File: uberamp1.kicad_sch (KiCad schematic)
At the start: 8 parts

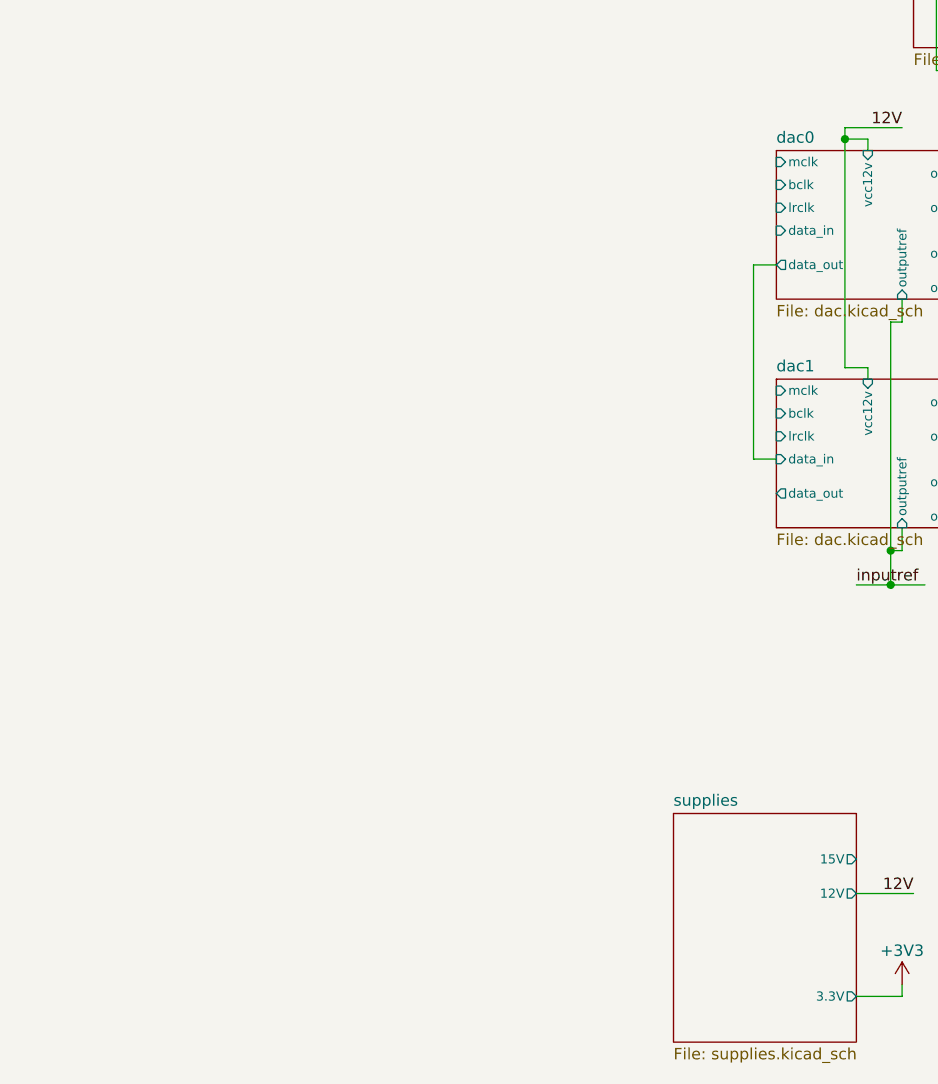
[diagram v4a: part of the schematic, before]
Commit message: add clock source to schematic
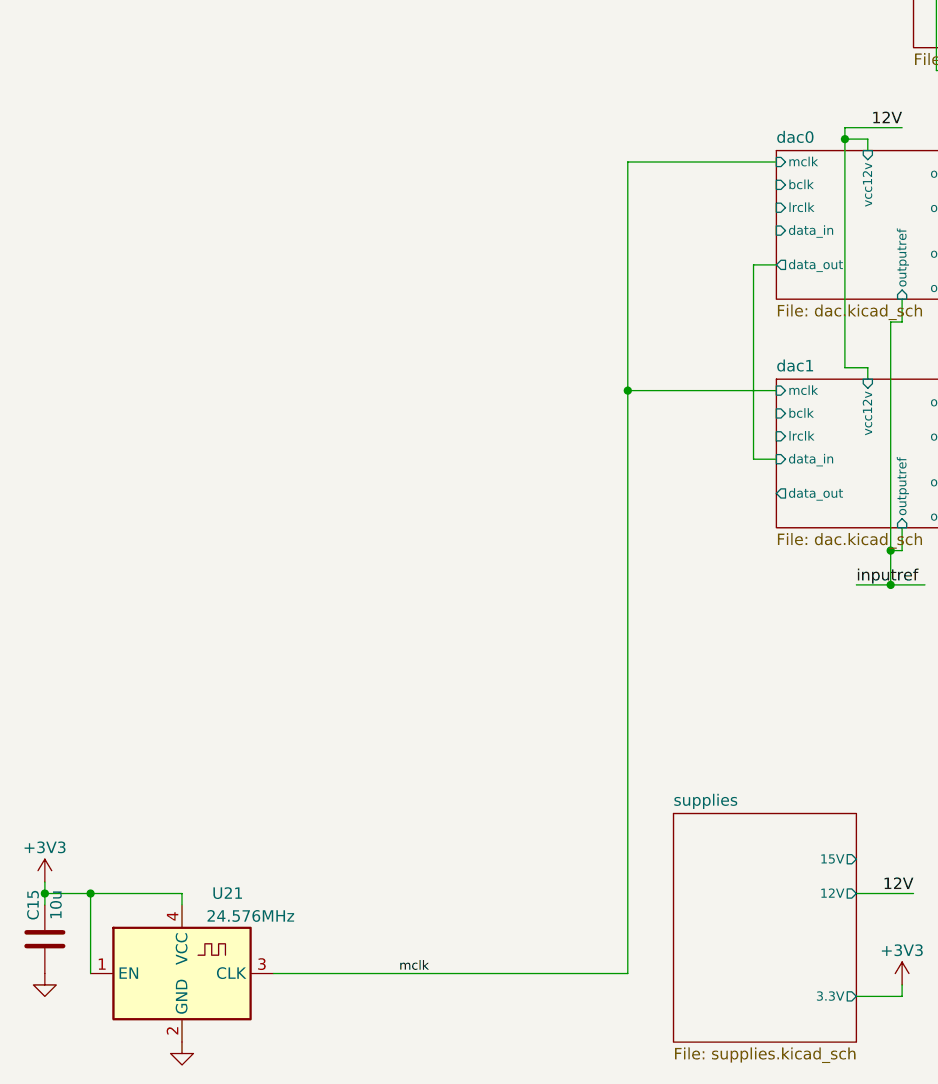
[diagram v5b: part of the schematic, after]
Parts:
- added C15: 10u, invendelirium_audio:C_0603, symbol Device:C
- added U21: 24.576MHz, symbol invendelirium_ic:kyocera_KC
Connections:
- net +3V3: now also C15.2, U21.1 (EN), U21.4 (VCC)
- net GND: now also C15.1, U21.2 (GND)
- new net mclk: U21.3 (CLK)
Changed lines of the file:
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@@
   (junction (at 186.69 113.03) (diameter 0) (color 0 0 0 0)
   )
+  (junction (at 119.38 111.76) (diameter 0) (color 0 0 0 0)
+  )
   (junction (at 209.55 92.71) (diameter 0) (color 0 0 0 0)
   )
@@
   (junction (at 210.82 21.59) (diameter 0) (color 0 0 0 0)
   )
+  (junction (at 54.61 167.64) (diameter 0) (color 0 0 0 0)
+  )
   (junction (at 189.23 76.2) (diameter 0) (color 0 0 0 0)
   )
@@
   )
   (junction (at 214.63 90.17) (diameter 0) (color 0 0 0 0)
+  )
+  (junction (at 59.69 167.64) (diameter 0) (color 0 0 0 0)
   )
   (junction (at 189.23 54.61) (diameter 0) (color 0 0 0 0)
@@
     (stroke (width 0) (type default))
   )
+  (wire (pts (xy 59.69 167.64) (xy 54.61 167.64))
+    (stroke (width 0) (type default))
+  )
   (wire (pts (xy 247.65 91.44) (xy 247.65 95.25))
     (stroke (width 0) (type default))
@@
     (stroke (width 0) (type default))
   )
+  (wire (pts (xy 119.38 111.76) (xy 135.89 111.76))
+    (stroke (width 0) (type default))
+  )
   (wire (pts (xy 194.31 105.41) (xy 194.31 71.12))
     (stroke (width 0) (type default))
@@
     (stroke (width 0) (type default))
   )
+  (wire (pts (xy 59.69 167.64) (xy 59.69 176.53))
+    (stroke (width 0) (type default))
+  )
   (wire (pts (xy 214.63 125.73) (xy 214.63 160.02))
     (stroke (width 0) (type default))
@@
     (stroke (width 0) (type default))
   )
+  (wire (pts (xy 54.61 166.37) (xy 54.61 167.64))
+    (stroke (width 0) (type default))
+  )
   (wire (pts (xy 246.38 146.05) (xy 247.65 146.05))
     (stroke (width 0) (type default))
@@
     (stroke (width 0) (type default))
   )
+  (wire (pts (xy 119.38 176.53) (xy 119.38 111.76))
+    (stroke (width 0) (type default))
+  )
   (wire (pts (xy 165.1 25.4) (xy 191.77 25.4))
     (stroke (width 0) (type default))
@@
     (stroke (width 0) (type default))
   )
+  (wire (pts (xy 135.89 86.36) (xy 119.38 86.36))
+    (stroke (width 0) (type default))
+  )
   (wire (pts (xy 198.12 142.24) (xy 191.77 142.24))
     (stroke (width 0) (type default))
@@
     (stroke (width 0) (type default))
   )
+  (wire (pts (xy 80.01 176.53) (xy 119.38 176.53))
+    (stroke (width 0) (type default))
+  )
   (wire (pts (xy 191.77 25.4) (xy 191.77 39.37))
     (stroke (width 0) (type default))
@@
     (stroke (width 0) (type default))
   )
+  (wire (pts (xy 119.38 86.36) (xy 119.38 111.76))
+    (stroke (width 0) (type default))
+  )
   (wire (pts (xy 166.37 113.03) (xy 181.61 113.03))
     (stroke (width 0) (type default))
@@
     (stroke (width 0) (type default))
   )
+  (wire (pts (xy 54.61 167.64) (xy 54.61 168.91))
+    (stroke (width 0) (type default))
+  )
   (wire (pts (xy 227.33 96.52) (xy 227.33 92.71))
     (stroke (width 0) (type default))
@@
     (stroke (width 0) (type default))
   )
+  (wire (pts (xy 69.85 168.91) (xy 69.85 167.64))
+    (stroke (width 0) (type default))
+  )
   (wire (pts (xy 212.09 129.54) (xy 212.09 127))
     (stroke (width 0) (type default))
   )
   (wire (pts (xy 212.09 58.42) (xy 209.55 58.42))
+    (stroke (width 0) (type default))
+  )
+  (wire (pts (xy 69.85 167.64) (xy 59.69 167.64))
     (stroke (width 0) (type default))
   )
@@
   (label "12V" (at 163.83 13.97 180) (fields_autoplaced)
     (effects (font (size 1.27 1.27)) (justify right bottom))
+  )
+  (label "mclk" (at 93.98 176.53 0) (fields_autoplaced)
+    (effects (font (size 1.016 1.016)) (justify left bottom))
   )
   (label "12V" (at 149.86 82.55 180) (fields_autoplaced)
@@
     )
   )
+  (symbol (lib_id "power:+3V3") (at 54.61 166.37 0) (unit 1)
+    (in_bom yes) (on_board yes) (dnp no) (fields_autoplaced)
+    (property "Reference" "#PWR092" (at 54.61 170.18 0)
+      (effects (font (size 1.27 1.27)) hide)
+    )
+    (property "Value" "+3V3" (at 54.61 162.56 0)
+      (effects (font (size 1.27 1.27)))
+    )
+    (property "Footprint" "" (at 54.61 166.37 0)
+      (effects (font (size 1.27 1.27)) hide)
+    )
+    (property "Datasheet" "" (at 54.61 166.37 0)
+      (effects (font (size 1.27 1.27)) hide)
+    )
+    (pin "1")
+    (instances
+      (project "uberamp1"
+        (path "/310059c1-d84b-43e2-9c9a-0e426c534a12/9338c448-a5fc-4246-a946-e7fc08f9b36f"
+          (reference "#PWR092") (unit 1)
+        )
+        (path "/310059c1-d84b-43e2-9c9a-0e426c534a12/7069641c-0ed4-4995-a63e-1f44999c4edd"
+          (reference "#PWR0115") (unit 1)
+        )
+        (path "/310059c1-d84b-43e2-9c9a-0e426c534a12"
+          (reference "#PWR0144") (unit 1)
+        )
+      )
+    )
+  )
+  (symbol (lib_id "power:GND") (at 54.61 176.53 0) (unit 1)
+    (in_bom yes) (on_board yes) (dnp no) (fields_autoplaced)
+    (property "Reference" "#PWR02" (at 54.61 182.88 0)
+      (effects (font (size 1.27 1.27)) hide)
+    )
+    (property "Value" "GND" (at 54.61 181.61 0)
+      (effects (font (size 1.27 1.27)) hide)
+    )
+    (property "Footprint" "" (at 54.61 176.53 0)
+      (effects (font (size 1.27 1.27)) hide)
+    )
+    (property "Datasheet" "" (at 54.61 176.53 0)
+      (effects (font (size 1.27 1.27)) hide)
+    )
+    (pin "1")
+    (instances
+      (project "uberamp1"
+        (path "/310059c1-d84b-43e2-9c9a-0e426c534a12/c6ef957f-dbb4-496d-aec2-44492c2243c4"
+          (reference "#PWR02") (unit 1)
+        )
+        (path "/310059c1-d84b-43e2-9c9a-0e426c534a12/1727f815-1282-4ad8-874c-d1f66f4d7fbe"
+          (reference "#PWR070") (unit 1)
+        )
+        (path "/310059c1-d84b-43e2-9c9a-0e426c534a12/e09aca01-5377-42b6-85e8-8afbf1155690"
+          (reference "#PWR071") (unit 1)
+        )
+        (path "/310059c1-d84b-43e2-9c9a-0e426c534a12/b23c2595-3b45-43cf-b3fd-b0c94e6d7f84"
+          (reference "#PWR072") (unit 1)
+        )
+        (path "/310059c1-d84b-43e2-9c9a-0e426c534a12"
+          (reference "#PWR0145") (unit 1)
+        )
+      )
+    )
+  )
+  (symbol (lib_id "power:GND") (at 69.85 184.15 0) (unit 1)
+    (in_bom yes) (on_board yes) (dnp no) (fields_autoplaced)
+    (property "Reference" "#PWR02" (at 69.85 190.5 0)
+      (effects (font (size 1.27 1.27)) hide)
+    )
+    (property "Value" "GND" (at 69.85 189.23 0)
+      (effects (font (size 1.27 1.27)) hide)
+    )
+    (property "Footprint" "" (at 69.85 184.15 0)
+      (effects (font (size 1.27 1.27)) hide)
+    )
+    (property "Datasheet" "" (at 69.85 184.15 0)
+      (effects (font (size 1.27 1.27)) hide)
+    )
+    (pin "1")
+    (instances
+      (project "uberamp1"
+        (path "/310059c1-d84b-43e2-9c9a-0e426c534a12/c6ef957f-dbb4-496d-aec2-44492c2243c4"
+          (reference "#PWR02") (unit 1)
+        )
+        (path "/310059c1-d84b-43e2-9c9a-0e426c534a12/1727f815-1282-4ad8-874c-d1f66f4d7fbe"
+          (reference "#PWR070") (unit 1)
+        )
+        (path "/310059c1-d84b-43e2-9c9a-0e426c534a12/e09aca01-5377-42b6-85e8-8afbf1155690"
+          (reference "#PWR071") (unit 1)
+        )
+        (path "/310059c1-d84b-43e2-9c9a-0e426c534a12/b23c2595-3b45-43cf-b3fd-b0c94e6d7f84"
+          (reference "#PWR072") (unit 1)
+        )
+        (path "/310059c1-d84b-43e2-9c9a-0e426c534a12"
+          (reference "#PWR0146") (unit 1)
+        )
+      )
+    )
+  )
   (symbol (lib_id "Device:C") (at 171.45 100.33 90) (unit 1)
     (in_bom yes) (on_board yes) (dnp no)
@@
     )
   )
+  (symbol (lib_id "Device:C") (at 54.61 172.72 180) (unit 1)
+    (in_bom yes) (on_board yes) (dnp no)
+    (property "Reference" "C15" (at 53.34 168.91 90)
+      (effects (font (size 1.27 1.27)))
+    )
+    (property "Value" "10u" (at 55.88 168.91 90)
+      (effects (font (size 1.27 1.27)))
+    )
+    (property "Footprint" "invendelirium_audio:C_0603" (at 53.6448 168.91 0)
+      (effects (font (size 1.27 1.27)) hide)
+    )
+    (property "Datasheet" "~" (at 54.61 172.72 0)
+      (effects (font (size 1.27 1.27)) hide)
+    )
+    (property "Voltage" "16V" (at 54.61 172.72 0)
+      (effects (font (size 1.27 1.27)) hide)
+    )
+    (pin "1")
+    (pin "2")
+    (instances
+      (project "uberamp1"
+        (path "/310059c1-d84b-43e2-9c9a-0e426c534a12/5156a0a1-195e-40e3-846d-487893ba8fa7"
+          (reference "C15") (unit 1)
+        )
+        (path "/310059c1-d84b-43e2-9c9a-0e426c534a12/f0f90934-0ffc-42c4-856c-3b886cd79d06"
+          (reference "C37") (unit 1)
+        )
+        (path "/310059c1-d84b-43e2-9c9a-0e426c534a12"
+          (reference "CU21") (unit 1)
+        )
+      )
+    )
+  )
   (symbol (lib_id "Device:C") (at 171.45 91.44 90) (unit 1)
     (in_bom yes) (on_board yes) (dnp no)
@@
         )
       )
+    )
+  )
+  (symbol (lib_id "invendelirium_ic:kyocera_KC") (at 69.85 176.53 0) (unit 1)
+    (in_bom yes) (on_board yes) (dnp no)
+    (property "Reference" "U21" (at 74.93 167.64 0)
+      (effects (font (size 1.27 1.27)))
+    )
+    (property "Value" "24.576MHz" (at 77.47 170.18 0)
+      (effects (font (size 1.27 1.27)))
+    )
+    (property "Footprint" "" (at 73.66 172.72 0)
+      (effects (font (size 1.27 1.27)) hide)
+    )
+    (property "Datasheet" "https://global.kyocera.com/prdct/electro/product/pdf/clock_z_xz_e.pdf" (at 73.66 172.72 0)
+      (effects (font (size 1.27 1.27)) hide)
+    )
+    (property "PN" "" (at 69.85 176.53 0)
+      (effects (font (size 1.27 1.27)))
+    )
+    (pin "1")
+    (pin "2")
+    (pin "3")
+    (pin "4")
+    (instances
+      (project "uberamp1"
+        (path "/310059c1-d84b-43e2-9c9a-0e426c534a12"
+          (reference "U21") (unit 1)
+        )
+      )

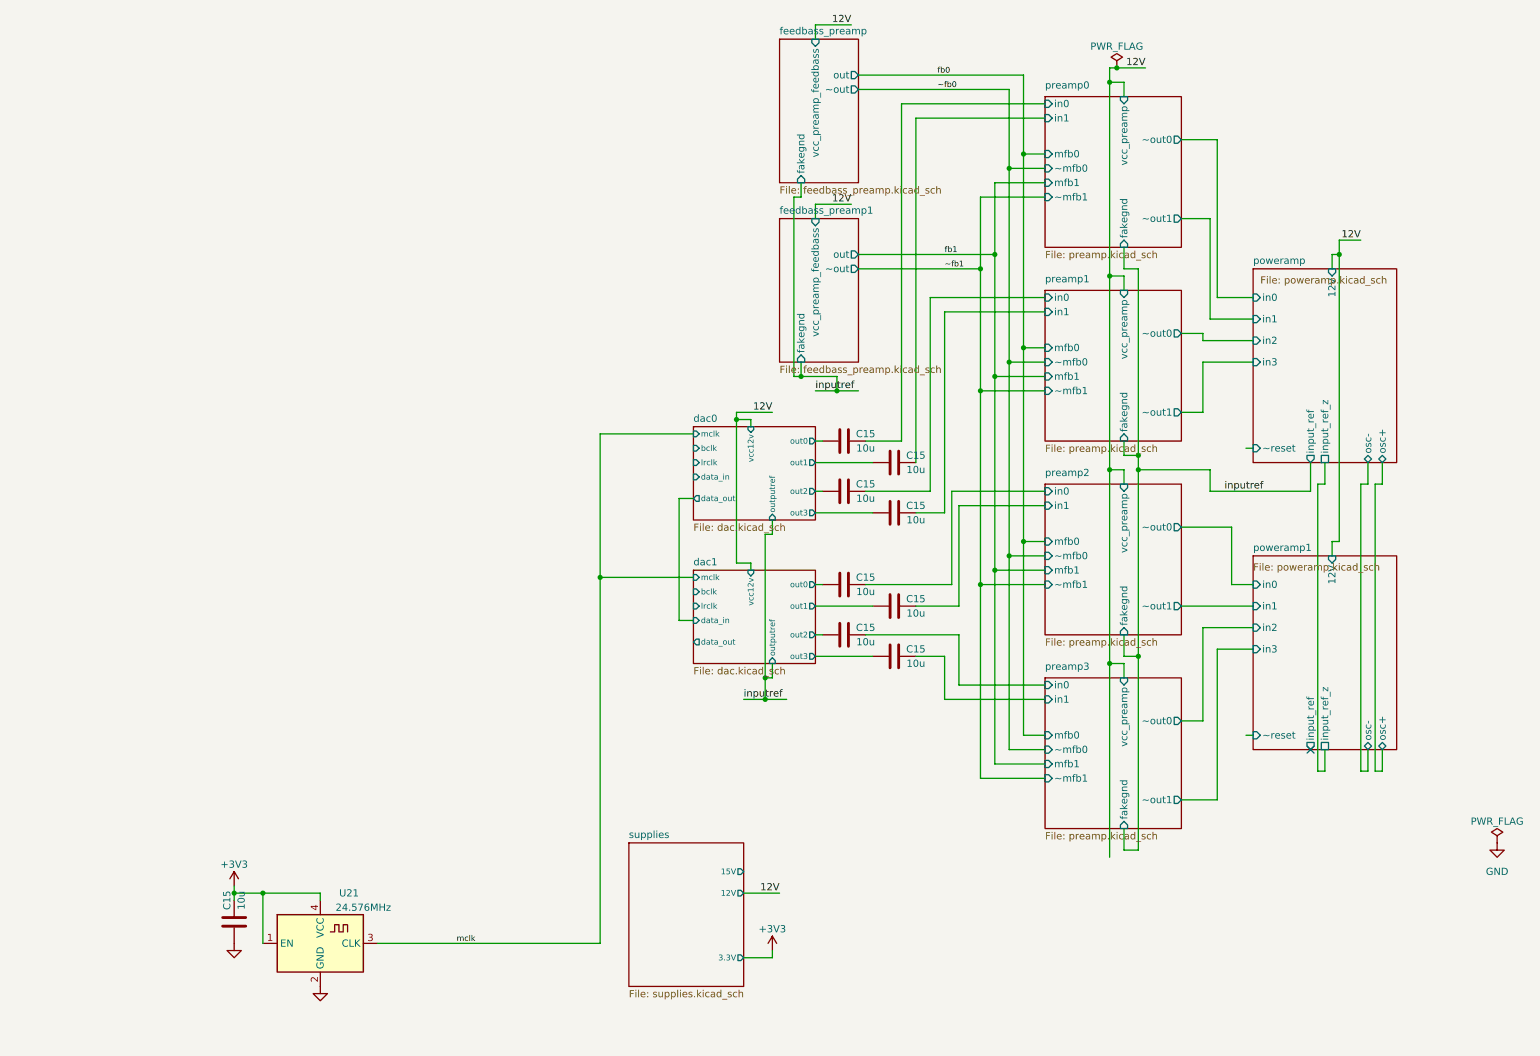
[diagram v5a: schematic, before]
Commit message: add dsp and esp32... schematic mostly done
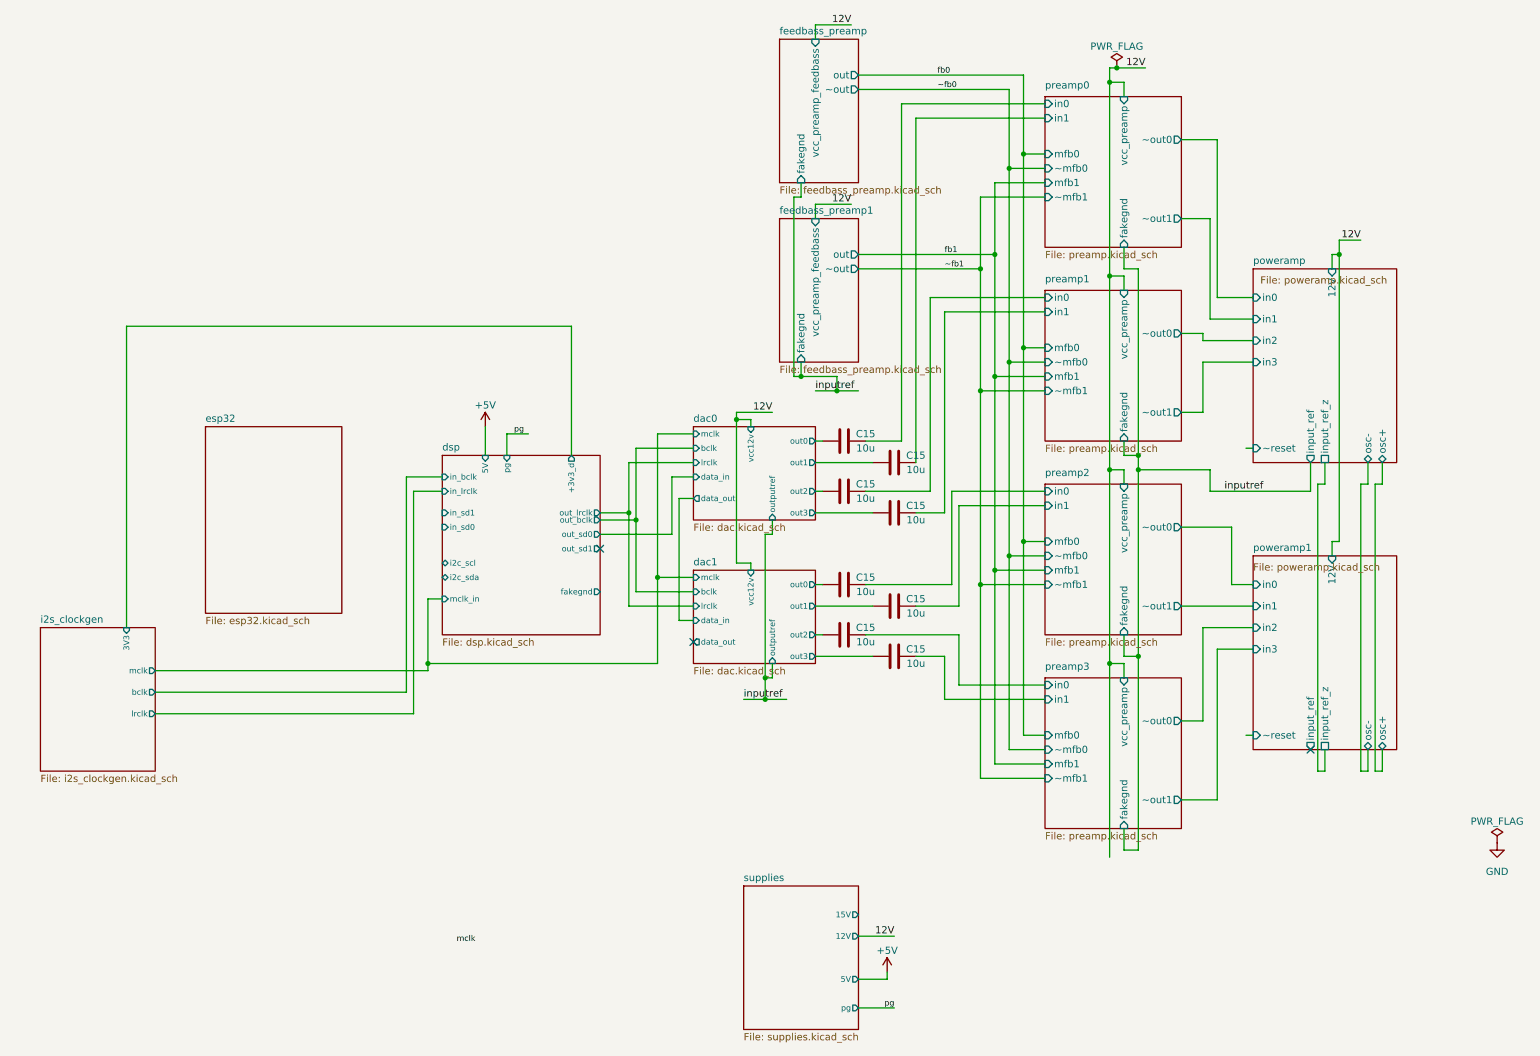
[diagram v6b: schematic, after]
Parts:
- removed C15: 10u, invendelirium_audio:C_0603, symbol Device:C
- removed U21: 24.576MHz, symbol invendelirium_ic:kyocera_KC
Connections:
- no-connect marks 1 -> 3
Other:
- added sheet dsp (dsp.kicad_sch)
- added sheet esp32 (esp32.kicad_sch)
- added sheet i2s_clockgen (i2s_clockgen.kicad_sch)
- sheet supplies ports: added 5V, pg; removed 3.3V
